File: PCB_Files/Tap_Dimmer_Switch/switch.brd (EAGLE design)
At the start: 91.2 x 90.7 mm, 37 parts, among them P1 HT7333

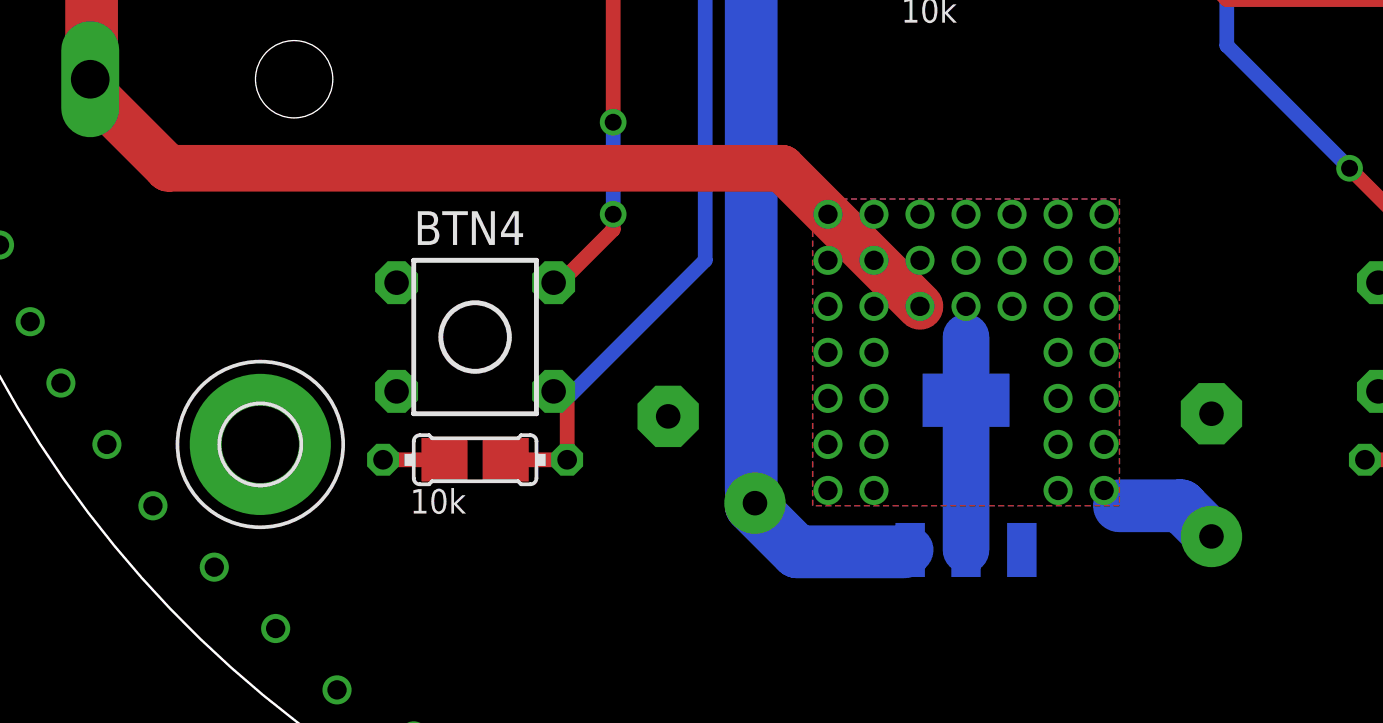
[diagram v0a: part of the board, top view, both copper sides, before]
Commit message: created additional compact design of ws2812b module
this new design features smaller footprint, but the esp module ist partially outside the board, which will result in better wifi connection.

additionally the footprint of the HT7333 has been fixed as previously it had used the wrong package.
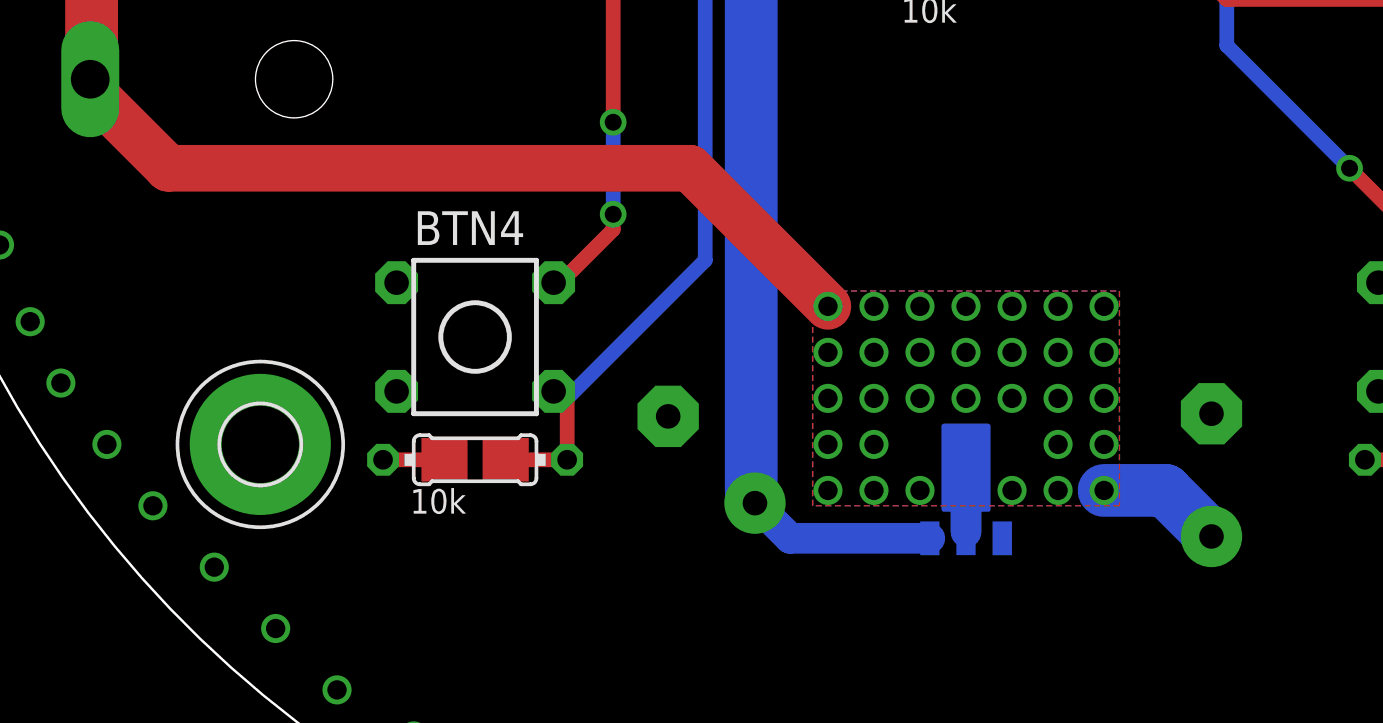
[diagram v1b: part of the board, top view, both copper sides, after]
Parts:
- P1: value HT7333 -> HT7333SOT89; device diyHue:SOT223 -> diyHue:SOT89
- moved P1 0.64 mm to (0.00, -26.7)
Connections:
- net +5V: now also P1.2@1; no longer P1.4
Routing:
- net +5V: track 70.9 -> 61.9 mm, vias 37 -> 31
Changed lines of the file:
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@@
 <element name="R12" library="diyHue" package="MULTI_RESISTOR" value="10k" x="-5.08" y="10.795" rot="R270"/>
 <element name="C1" library="rcl" package="C025-025X050" value="10nF" x="17.78" y="6.35" rot="R180"/>
-<element name="P1" library="diyHue" package="SOT223" value="HT7333" x="0" y="-26.035" rot="MR0"/>
+<element name="P1" library="diyHue" package="SOT89" value="HT7333SOT89" x="0" y="-26.67" rot="MR0"/>
 <element name="FTDI" library="pinhead-2" package="1X06-S" value="" x="19.05" y="33.02" smashed="yes" rot="MR0">
 <attribute name="NAME" x="26.7462" y="30.0863" size="1.27" layer="26" font="vector" ratio="10" rot="MR0"/>
@@
 <contactref element="P1" pad="2"/>
 <contactref element="C3" pad="+"/>
-<contactref element="P1" pad="4"/>
-<wire x1="0" y1="-22.936" x2="0" y2="-29.1338" width="1.9304" layer="16"/>
-<wire x1="0" y1="-22.936" x2="0" y2="-20.32" width="1.9304" layer="16"/>
-<wire x1="-7.62" y1="-13.335" x2="-1.905" y2="-19.05" width="1.9304" layer="1"/>
-<wire x1="-33.02" y1="-13.335" x2="-7.62" y2="-13.335" width="1.9304" layer="1"/>
+<contactref element="P1" pad="2@1"/>
+<wire x1="-11.43" y1="-13.335" x2="-5.715" y2="-19.05" width="1.9304" layer="1"/>
+<wire x1="-33.02" y1="-13.335" x2="-11.43" y2="-13.335" width="1.9304" layer="1"/>
 <wire x1="-36.195" y1="-10.16" x2="-33.02" y2="-13.335" width="1.9304" layer="1"/>
 <wire x1="-36.195" y1="-10.16" x2="-36.25" y2="-9.65" width="1.9304" layer="1"/>
 <polygon width="0.6096" layer="16">
-<vertex x="-6.35" y="-14.605"/>
-<vertex x="6.35" y="-14.605"/>
+<vertex x="-6.35" y="-18.415"/>
+<vertex x="6.35" y="-18.415"/>
 <vertex x="6.35" y="-27.305"/>
 <vertex x="-6.35" y="-27.305"/>
 </polygon>
-<wire x1="8.89" y1="-27.305" x2="6.35" y2="-27.305" width="2.1844" layer="16"/>
-<wire x1="10.16" y1="-28.575" x2="8.89" y2="-27.305" width="2.1844" layer="16"/>
+<wire x1="8.255" y1="-26.67" x2="5.715" y2="-26.67" width="2.1844" layer="16"/>
+<wire x1="10.16" y1="-28.575" x2="8.255" y2="-26.67" width="2.1844" layer="16"/>
 <polygon width="0.6096" layer="1">
-<vertex x="-6.35" y="-14.605"/>
-<vertex x="6.35" y="-14.605"/>
+<vertex x="-6.35" y="-18.415"/>
+<vertex x="6.35" y="-18.415"/>
 <vertex x="6.35" y="-27.305"/>
 <vertex x="-6.35" y="-27.305"/>
 </polygon>
-<via x="-5.715" y="-15.24" extent="1-16" drill="0.8"/>
-<via x="-3.81" y="-15.24" extent="1-16" drill="0.8"/>
-<via x="-1.905" y="-15.24" extent="1-16" drill="0.8"/>
-<via x="0" y="-15.24" extent="1-16" drill="0.8"/>
-<via x="1.905" y="-15.24" extent="1-16" drill="0.8"/>
-<via x="3.81" y="-15.24" extent="1-16" drill="0.8"/>
-<via x="5.715" y="-15.24" extent="1-16" drill="0.8"/>
-<via x="5.715" y="-17.145" extent="1-16" drill="0.8"/>
-<via x="3.81" y="-17.145" extent="1-16" drill="0.8"/>
-<via x="1.905" y="-17.145" extent="1-16" drill="0.8"/>
-<via x="0" y="-17.145" extent="1-16" drill="0.8"/>
-<via x="-1.905" y="-17.145" extent="1-16" drill="0.8"/>
-<via x="-3.81" y="-17.145" extent="1-16" drill="0.8"/>
-<via x="-5.715" y="-17.145" extent="1-16" drill="0.8"/>
+<via x="1.905" y="-26.67" extent="1-16" drill="0.8"/>
+<via x="-1.905" y="-26.67" extent="1-16" drill="0.8"/>
+<via x="-1.905" y="-22.86" extent="1-16" drill="0.8"/>
+<via x="0" y="-22.86" extent="1-16" drill="0.8"/>
+<via x="1.905" y="-22.86" extent="1-16" drill="0.8"/>
+<via x="1.905" y="-20.955" extent="1-16" drill="0.8"/>
+<via x="0" y="-20.955" extent="1-16" drill="0.8"/>
+<via x="-1.905" y="-20.955" extent="1-16" drill="0.8"/>
+<via x="-1.905" y="-19.05" extent="1-16" drill="0.8"/>
+<via x="-3.81" y="-19.05" extent="1-16" drill="0.8"/>
 <via x="-5.715" y="-19.05" extent="1-16" drill="0.8"/>
-<via x="-3.81" y="-19.05" extent="1-16" drill="0.8"/>
-<via x="-1.905" y="-19.05" extent="1-16" drill="0.8"/>
 <via x="0" y="-19.05" extent="1-16" drill="0.8"/>
 <via x="1.905" y="-19.05" extent="1-16" drill="0.8"/>
@@
 <wire x1="-36.195" y1="-8.89" x2="-36.25" y2="-9.65" width="2.1844" layer="1"/>
 <wire x1="-36.195" y1="9.525" x2="-36.25" y2="9.65" width="2.1844" layer="1"/>
+<wire x1="0" y1="-28.397" x2="0" y2="-25.73" width="1.27" layer="16"/>
 </signal>
 <signal name="RST">
@@
 <wire x1="19.685" y1="8.89" x2="23.495" y2="5.08" width="0.6096" layer="1"/>
 <wire x1="23.495" y1="5.08" x2="23.96" y2="4.76" width="0.6096" layer="1"/>
-<wire x1="-8.735921875" y1="-27.19605" x2="-8.89" y2="-27.305" width="2.1844" layer="16"/>
-<wire x1="-8.89" y1="-27.305" x2="-6.985" y2="-29.21" width="2.1844" layer="16"/>
-<wire x1="-6.985" y1="-29.21" x2="-2.54" y2="-29.21" width="2.1844" layer="16"/>
-<wire x1="-2.54" y1="-29.21" x2="-2.3114" y2="-29.1338" width="1.9304" layer="16"/>
 <wire x1="-8.89" y1="3.175" x2="-8.89" y2="-26.67" width="2.1844" layer="16"/>
 <wire x1="-5.08" y1="6.985" x2="-8.89" y2="3.175" width="2.1844" layer="16"/>
@@
 <wire x1="18.415" y1="32.385" x2="18.415" y2="30.48" width="0.6096" layer="16"/>
 <wire x1="17.78" y1="33.02" x2="18.415" y2="32.385" width="0.6096" layer="16"/>
+<wire x1="-1.499" y1="-28.651" x2="-7.280971875" y2="-28.651" width="1.27" layer="16"/>
+<wire x1="-7.280971875" y1="-28.651" x2="-8.735921875" y2="-27.19605" width="1.27" layer="16"/>
 </signal>
 <signal name="N$4">
